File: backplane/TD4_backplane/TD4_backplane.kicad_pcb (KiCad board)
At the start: 2 copper layers, 150 x 110 mm, 10 parts, among them J1 Conn_02x32_Row_Letter_First, J2 Conn_02x32_Row_Letter_First, J3 Conn_02x32_Row_Letter_First, J4 Conn_02x32_Row_Letter_First, J5 Conn_02x32_Row_Letter_First, J6 Barrel_Jack_Switch

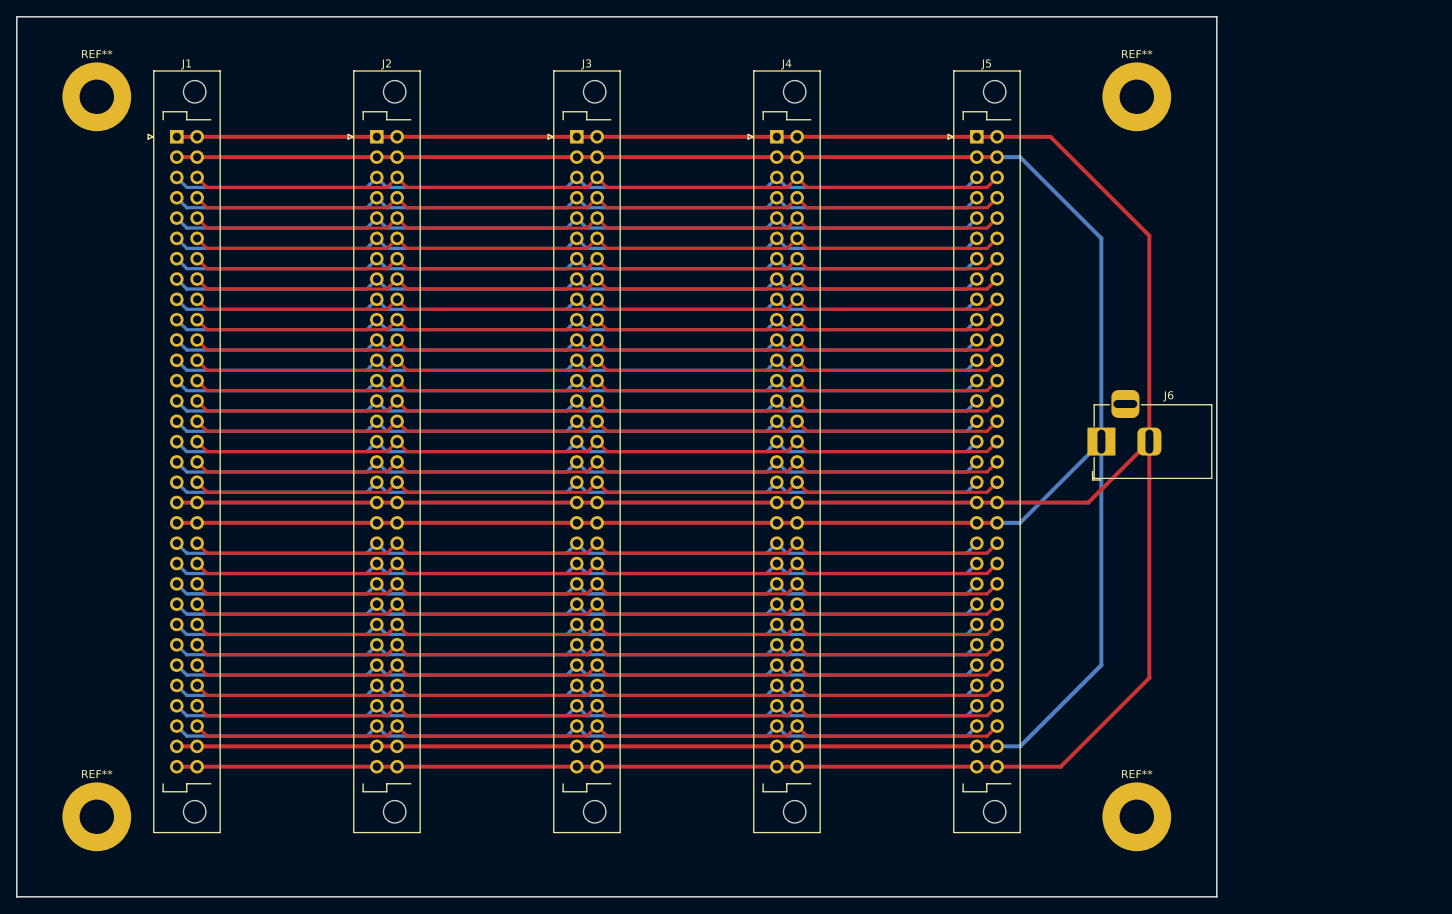
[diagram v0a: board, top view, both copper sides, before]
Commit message: Added 6th slot to the backplane
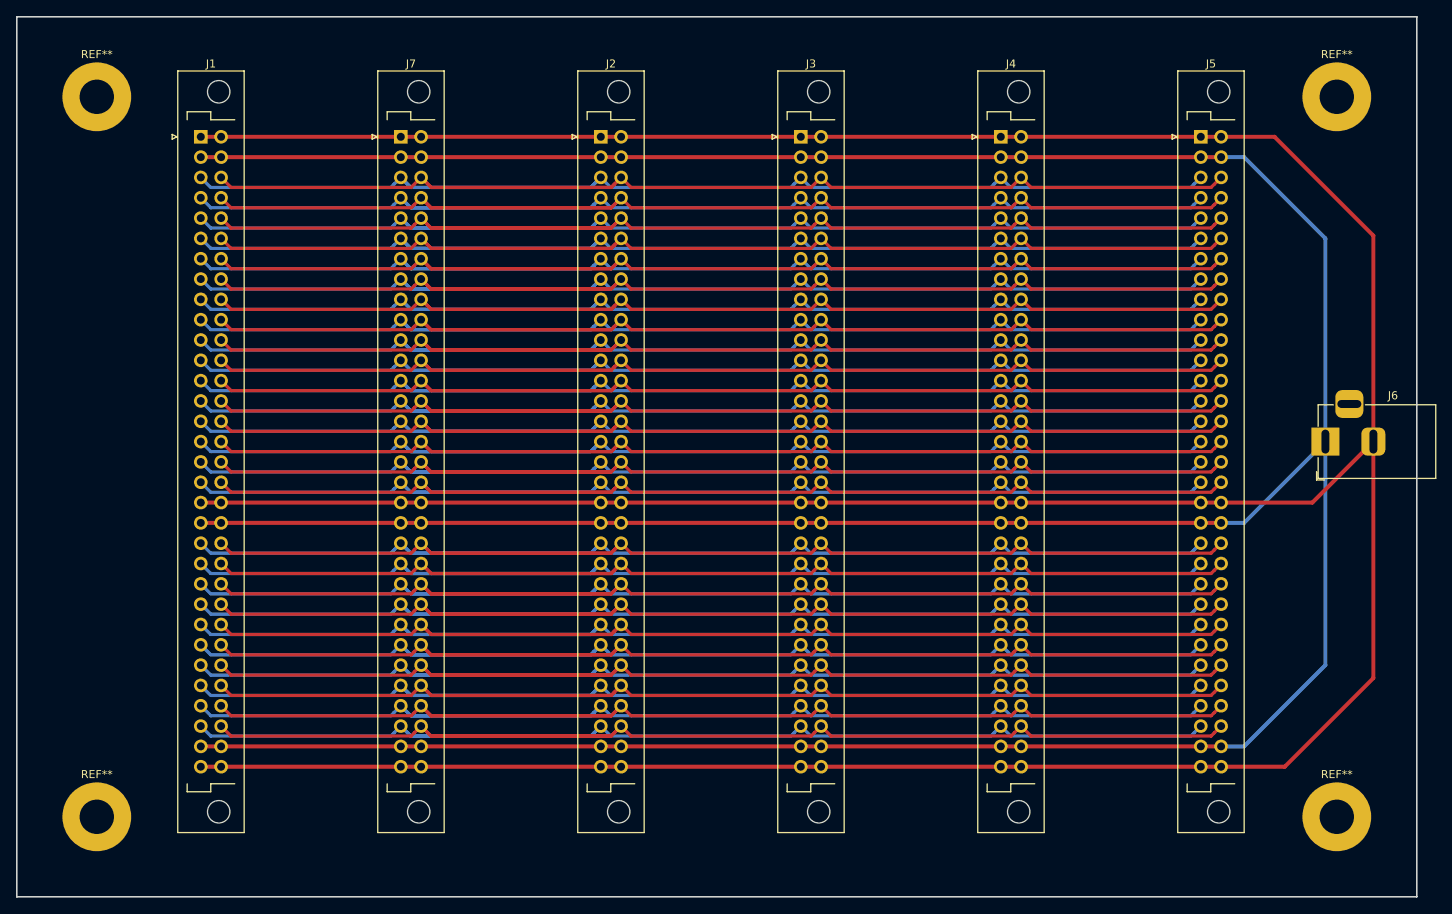
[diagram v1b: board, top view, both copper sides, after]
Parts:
- added J7: Conn_02x32_Row_Letter_First, Connector_DIN:DIN41612_B_2x32_Vertical, F.Cu at (83.0, 50.0)
- moved J2 28.0 mm to (108.0, 50.0)
- moved J3 28.0 mm to (133.0, 50.0)
- moved J4 28.0 mm to (158.0, 50.0)
- moved J5 28.0 mm to (183.0, 50.0)
- moved J6 28.0 mm to (198.6, 88.1)
- moved REF** 25.0 mm to (200.0, 135.0)
- moved REF** 25.0 mm to (200.0, 45.0)
- moved J1 3.00 mm to (58.0, 50.0)
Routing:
- net VCC: track 412.7 -> 487.7 mm
- net GND: track 432.9 -> 507.9 mm
- net /A38: track 104.1 -> 156.2 mm
- net /A47: track 104.1 -> 156.2 mm
- net /A40: track 104.1 -> 156.2 mm
- net /A35: track 104.1 -> 156.2 mm
- net /A34: track 104.1 -> 156.2 mm
- net /A3: track 104.1 -> 156.2 mm
- net /A27: track 104.1 -> 156.2 mm
- net /A25: track 104.1 -> 156.2 mm
- net /A24: track 104.1 -> 156.2 mm
- net /A11: track 104.1 -> 156.2 mm
- net /A10: track 104.1 -> 156.2 mm
- net /A9: track 104.1 -> 156.2 mm
- net /A8: track 104.1 -> 156.2 mm
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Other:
- board size 150 x 110 mm -> 175 x 110 mm
